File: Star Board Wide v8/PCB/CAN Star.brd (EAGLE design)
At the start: 221 x 38.1 mm, 12 parts

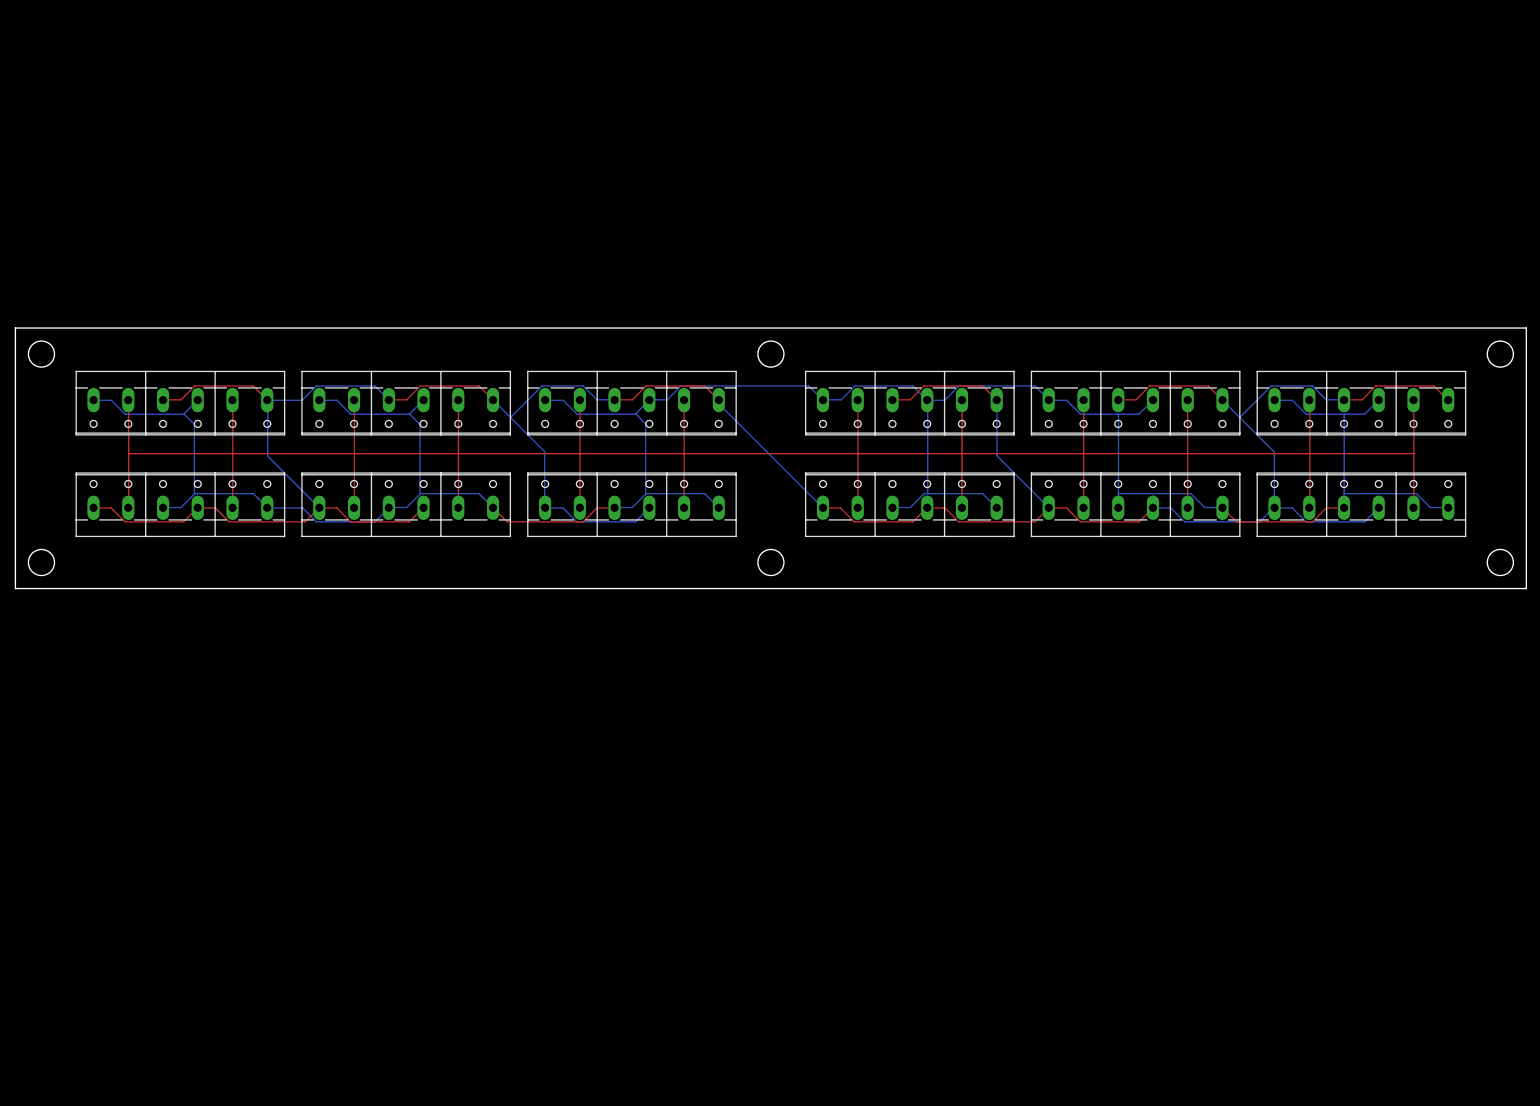
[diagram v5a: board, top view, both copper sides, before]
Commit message: Reduced lengh so that it'll be producible by custompbc.com
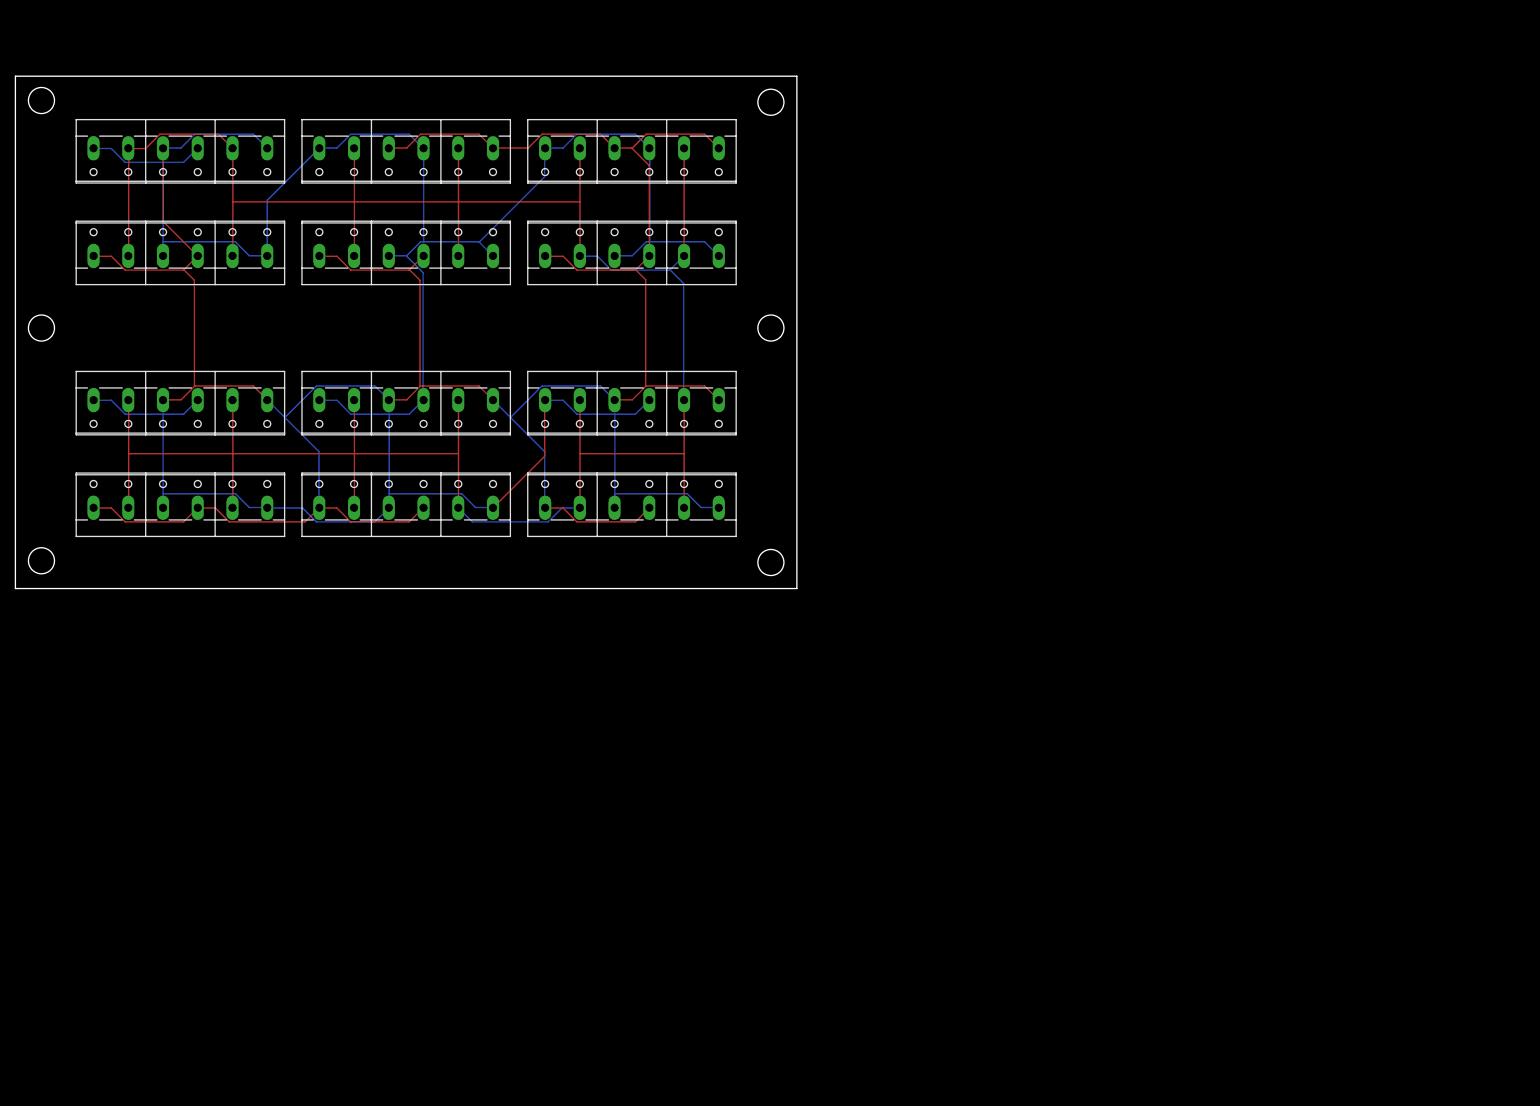
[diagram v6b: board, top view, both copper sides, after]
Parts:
- moved U$10 112.9 mm to (24.1, 61.2)
- moved U$11 112.9 mm to (57.1, 61.2)
- moved U$4 112.9 mm to (24.1, 51.8)
- moved U$5 112.9 mm to (57.1, 51.8)
- moved U$12 112.9 mm to (90.2, 61.2)
- moved U$6 112.9 mm to (90.2, 51.8)
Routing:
- net GND: track 415.2 -> 404.0 mm
- net G(L): track 384.9 -> 379.4 mm
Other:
- board size 221 x 38.1 mm -> 114.3 x 74.9 mm
